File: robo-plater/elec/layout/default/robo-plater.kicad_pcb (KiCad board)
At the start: 2 copper layers, 80 parts, among them U1 ?, U10 ?, U11 ?, U12 ?, U13 ?, U14 ?, U15 ?, U16 ?, U17 ?, U18 ?, U19 ?, U2 ?, U3 ?, U4 ?, U5 ?, U6 ?, U7 ?, U8 ?, U9 ?

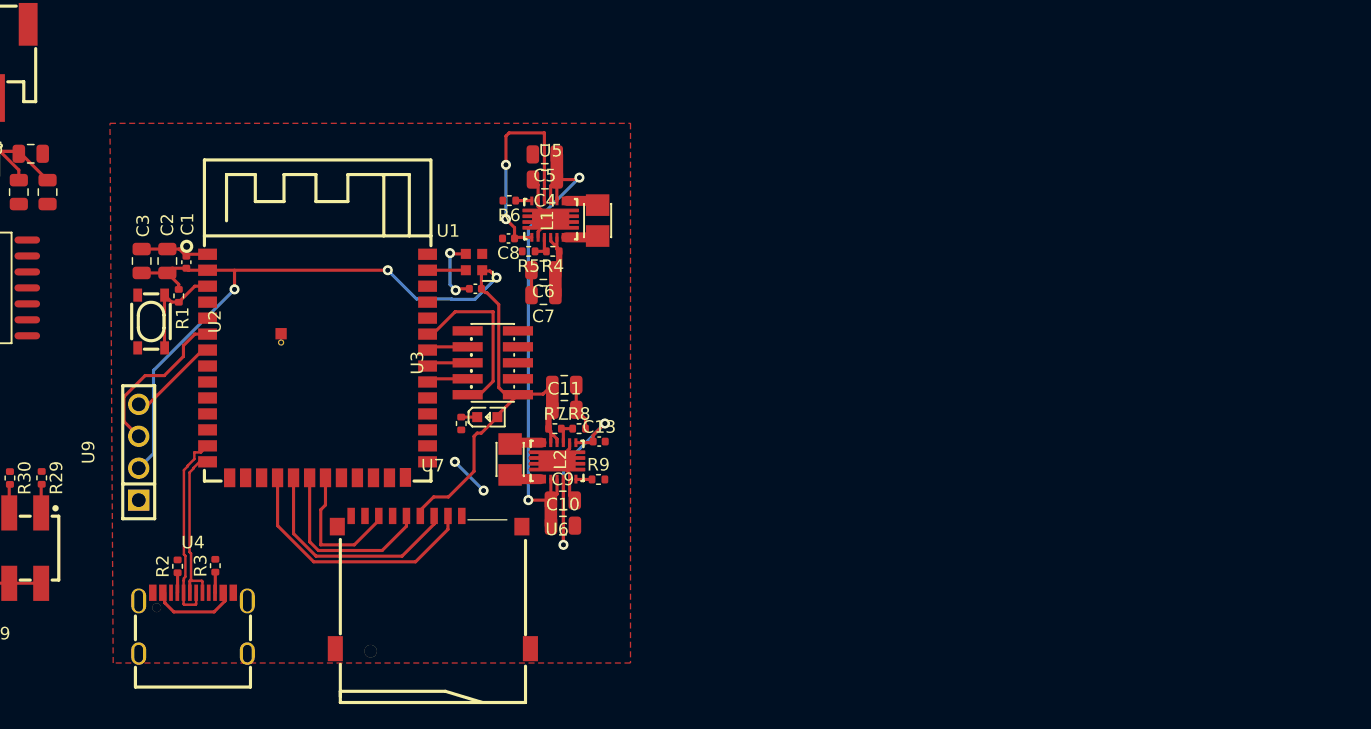
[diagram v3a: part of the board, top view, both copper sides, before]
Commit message: Add 12V input and power connector
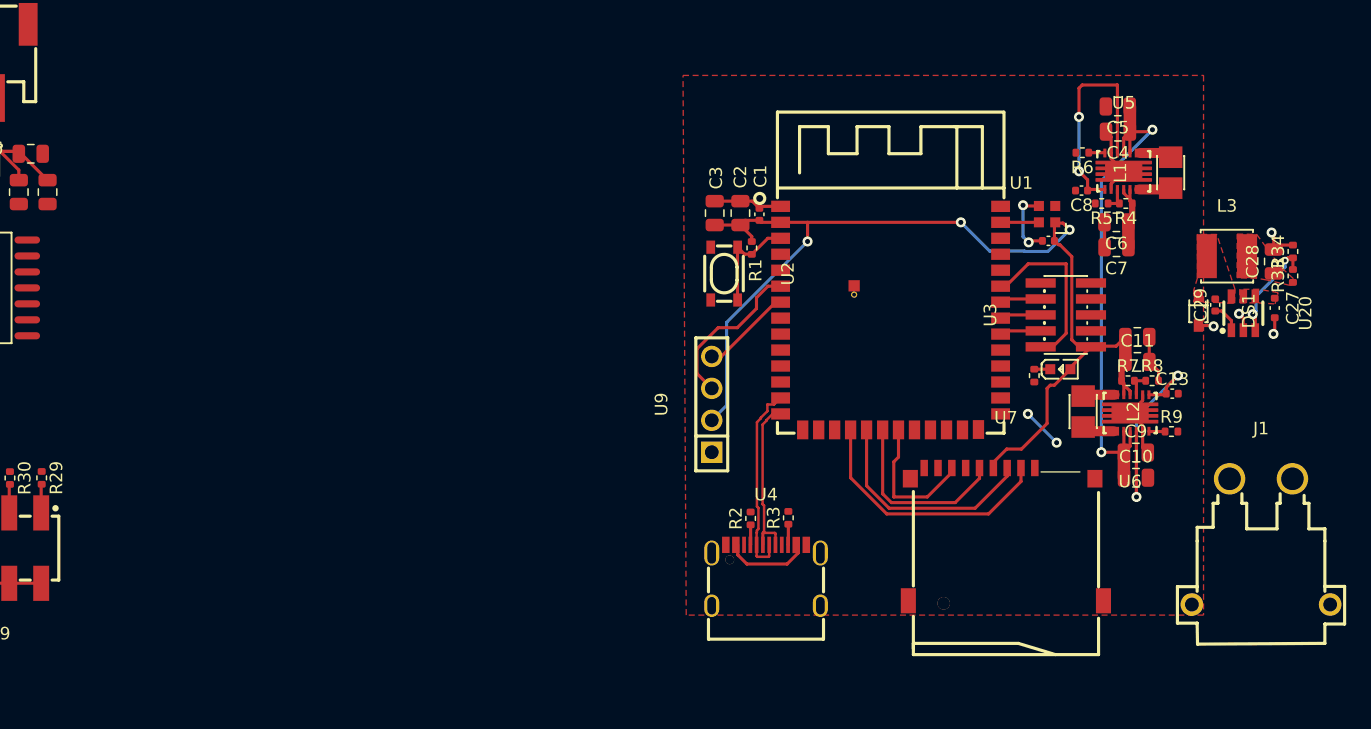
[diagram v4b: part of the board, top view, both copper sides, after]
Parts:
- added C27: 6.3V 10uF X5R ±20% 0402 Multilayer Ceramic Capacitors MLCC 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, lib:C0402, F.Cu at (196.4, 67.5)
- added C28: 25V 10uF X5R ±10% 0805 Multilayer Ceramic Capacitors MLCC -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, lib:C0805, F.Cu at (196.3, 63.8)
- added C29: 16V 100nF X7R ±10% 0402 Multilayer Ceramic Capacitors MLCC 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, lib:C0402, F.Cu at (191.7, 67.3)
- added DS1: ?, lib:SOD-323_L1.8-W1.3-LS2.5-RD, F.Cu at (190.3, 67.7)
- added J1: ?, lib:CONN-TH_XT30PW-M, F.Cu at (195.3, 86.1)
- added L3: ?, lib:IND-SMD_L4.0-W4.0, F.Cu at (192.6, 63.4)
- added R33: 62.5mW Thick Film Resistors 50V ±100ppm/℃ ±1% 23.7kΩ 0402 C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, lib:R0402, F.Cu at (197.9, 65.0)
- added R34: 62.5mW Thick Film Resistors 50V ±100ppm/℃ ±1% 4.3kΩ 0402 Ch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, lib:R0402, F.Cu at (197.9, 63.0)
- added U20: 0.6A, 42V, 1.1MHz Buck Regulator, lib:SOT-23-6_L2.9-W1.6-P0.95-LS2.8-BR, F.Cu at (193.9, 67.9)
- moved C12 45.7 mm to (185.5, 69.8)
- moved C13 45.7 mm to (188.3, 74.3)
- moved C2 45.7 mm to (153.9, 60.0)
- moved C6 45.7 mm to (183.8, 60.7)
- moved C9 45.7 mm to (185.4, 79.0)
- moved L1 45.7 mm to (188.1, 56.8)
- moved L2 45.7 mm to (181.2, 75.8)
- moved R1 45.7 mm to (154.8, 62.7)
- moved R10 45.7 mm to (177.3, 72.9)
- moved R4 45.7 mm to (184.6, 59.2)
- moved U3 45.7 mm to (179.8, 68.1)
- moved U6 45.7 mm to (184.9, 75.9)
- moved C1 45.7 mm to (155.4, 60.1)
- moved C3 45.7 mm to (151.9, 60.0)
- moved R2 45.7 mm to (154.7, 84.3)
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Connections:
- net uc.uc.ic-dm renamed ch2.pulses
- net uc.uc.ic-dm-1 renamed ch1.pulses
- net uc.uc.ic-dp renamed ch2.current
- net uc.uc.ic-dp-1 renamed ch1.current
- net uc.uc.ic-scl-2 renamed scl
- net uc.uc.ic-sda-2 renamed sda
- C1 pad 2: uc.uc.ic-gnd -> gnd
- C10 pad 2: uc.uc.ic-gnd -> gnd
- C11 pad 2: uc.uc.ic-gnd -> gnd
- C12 pad 2: uc.uc.ic-gnd -> gnd
- C13 pad 2: uc.uc.ic-gnd -> gnd
- C14 pad 2: uc.uc.ic-gnd -> gnd
- C2 pad 2: uc.uc.ic-gnd -> gnd
- C3 pad 2: uc.uc.ic-gnd -> gnd
- C4 pad 2: uc.uc.ic-gnd -> gnd
- C5 pad 2: uc.uc.ic-gnd -> gnd
- C6 pad 2: uc.uc.ic-gnd -> gnd
- C7 pad 2: uc.uc.ic-gnd -> gnd
- C8 pad 2: uc.uc.ic-gnd -> gnd
- C9 pad 2: uc.uc.ic-gnd -> gnd
- R10 pad 2: uc.uc.ic-gnd -> gnd
- R18 pad 1: uc.uc.ic-scl-1 -> ch1.dir
- R19 pad 1: uc.uc.ic-sda-1 -> ch1.pwm
- R2 pad 2: uc.uc.ic-gnd -> gnd
- R29 pad 1: uc.uc.ic-scl -> ch2.dir
- R3 pad 2: uc.uc.ic-gnd -> gnd
- R30 pad 1: uc.uc.ic-sda -> ch2.pwm
- R5 pad 2: uc.uc.ic-gnd -> gnd
- R6 pad 2: uc.uc.ic-gnd -> gnd
- R8 pad 2: uc.uc.ic-gnd -> gnd
- R9 pad 2: uc.uc.ic-gnd -> gnd
- U1 pad 1: uc.uc.ic-gnd -> gnd
- U1 pad 12: uc.uc.ic-sda -> ch2.dir
- U1 pad 15: uc.uc.ic-scl -> ch2.pwm
- U1 pad 40: uc.uc.ic-gnd -> gnd
- U1 pad 41: uc.uc.ic-gnd -> gnd
- U1 pad 8: uc.uc.ic-sda-1 -> ch1.dir
- U1 pad 9: uc.uc.ic-scl-1 -> ch1.pwm
- U10 pad 5: uc.uc.ic-scl-1 -> ch1.pwm
- U10 pad 6: uc.uc.ic-sda-1 -> ch1.dir
- U15 pad 5: uc.uc.ic-scl -> ch2.pwm
- U15 pad 6: uc.uc.ic-sda -> ch2.dir
- U2 pad 3: uc.uc.ic-gnd -> gnd
- U2 pad 4: uc.uc.ic-gnd -> gnd
- U3 pad 3: uc.uc.ic-gnd -> gnd
- U3 pad 5: uc.uc.ic-gnd -> gnd
- U3 pad 9: uc.uc.ic-gnd -> gnd
- U4 pad 1: uc.uc.ic-gnd -> gnd
- U4 pad 2: uc.uc.ic-gnd -> gnd
- U4 pad 3: uc.uc.ic-gnd -> gnd
- U4 pad 4: uc.uc.ic-gnd -> gnd
- U4 pad A1: uc.uc.ic-gnd -> gnd
- U4 pad A12: uc.uc.ic-gnd -> gnd
- U4 pad B1: uc.uc.ic-gnd -> gnd
- U4 pad B12: uc.uc.ic-gnd -> gnd
- U5 pad 13: uc.uc.ic-gnd -> gnd
- U5 pad 15: uc.uc.ic-gnd -> gnd
- U5 pad 2: uc.uc.ic-gnd -> gnd
- U6 pad 13: uc.uc.ic-gnd -> gnd
- U6 pad 15: uc.uc.ic-gnd -> gnd
- U6 pad 2: uc.uc.ic-gnd -> gnd
- U7 pad 10: uc.uc.ic-gnd -> gnd
- U7 pad 11: uc.uc.ic-gnd -> gnd
- U7 pad 12: uc.uc.ic-gnd -> gnd
- U7 pad 13: uc.uc.ic-gnd -> gnd
- U7 pad 6: uc.uc.ic-gnd -> gnd
- U8 pad 3: uc.uc.ic-gnd -> gnd
- U9 pad 1: uc.uc.ic-gnd -> gnd
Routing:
- net gnd: track 26.9 -> 62.0 mm, vias 0 -> 6
- net uc.uc.ic-gnd: track 28.1 -> 0.00 mm, vias 2 -> 0
- net uc.uc.ic-sda: track 14.2 -> 0.00 mm
- net ch2.dir: track 0.00 -> 14.2 mm
- net uc.uc.ic-sda-1: track 14.2 -> 0.00 mm
- net ch1.dir: track 0.00 -> 14.2 mm
- net uc.uc.ic-scl: track 14.2 -> 0.00 mm
- net ch2.pwm: track 0.00 -> 14.2 mm
- net uc.uc.ic-scl-1: track 14.2 -> 0.00 mm
- net ch1.pwm: track 0.00 -> 14.2 mm
- net supply_5v.feedback_div-out: track 0.00 -> 8.33 mm, vias 0 -> 2
- net cb: track 0.00 -> 2.36 mm
- added copper zone on F.Cu, net gnd
- added copper zone on F.Cu, net sw
- added copper zone on F.Cu, net uc-vcc
- added copper zone on F.Cu, net vcc
- removed copper zone on F.Cu, net uc.uc.ic-gnd

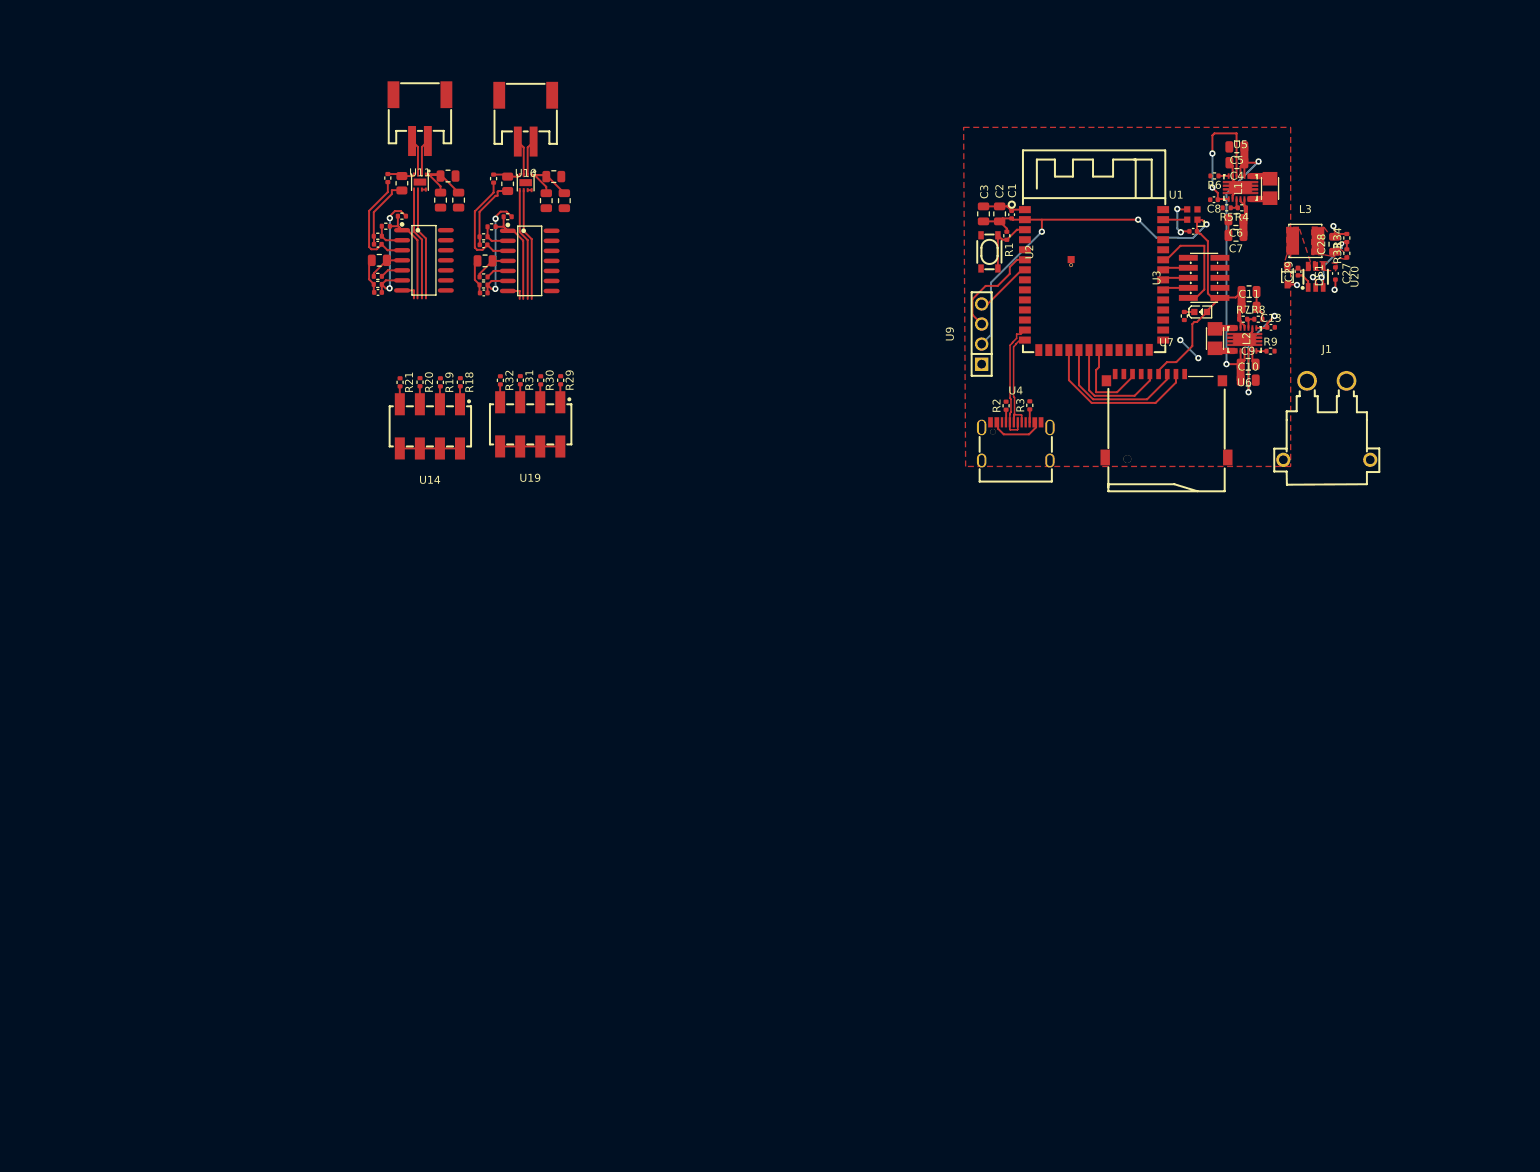
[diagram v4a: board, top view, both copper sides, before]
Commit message: Add io expander
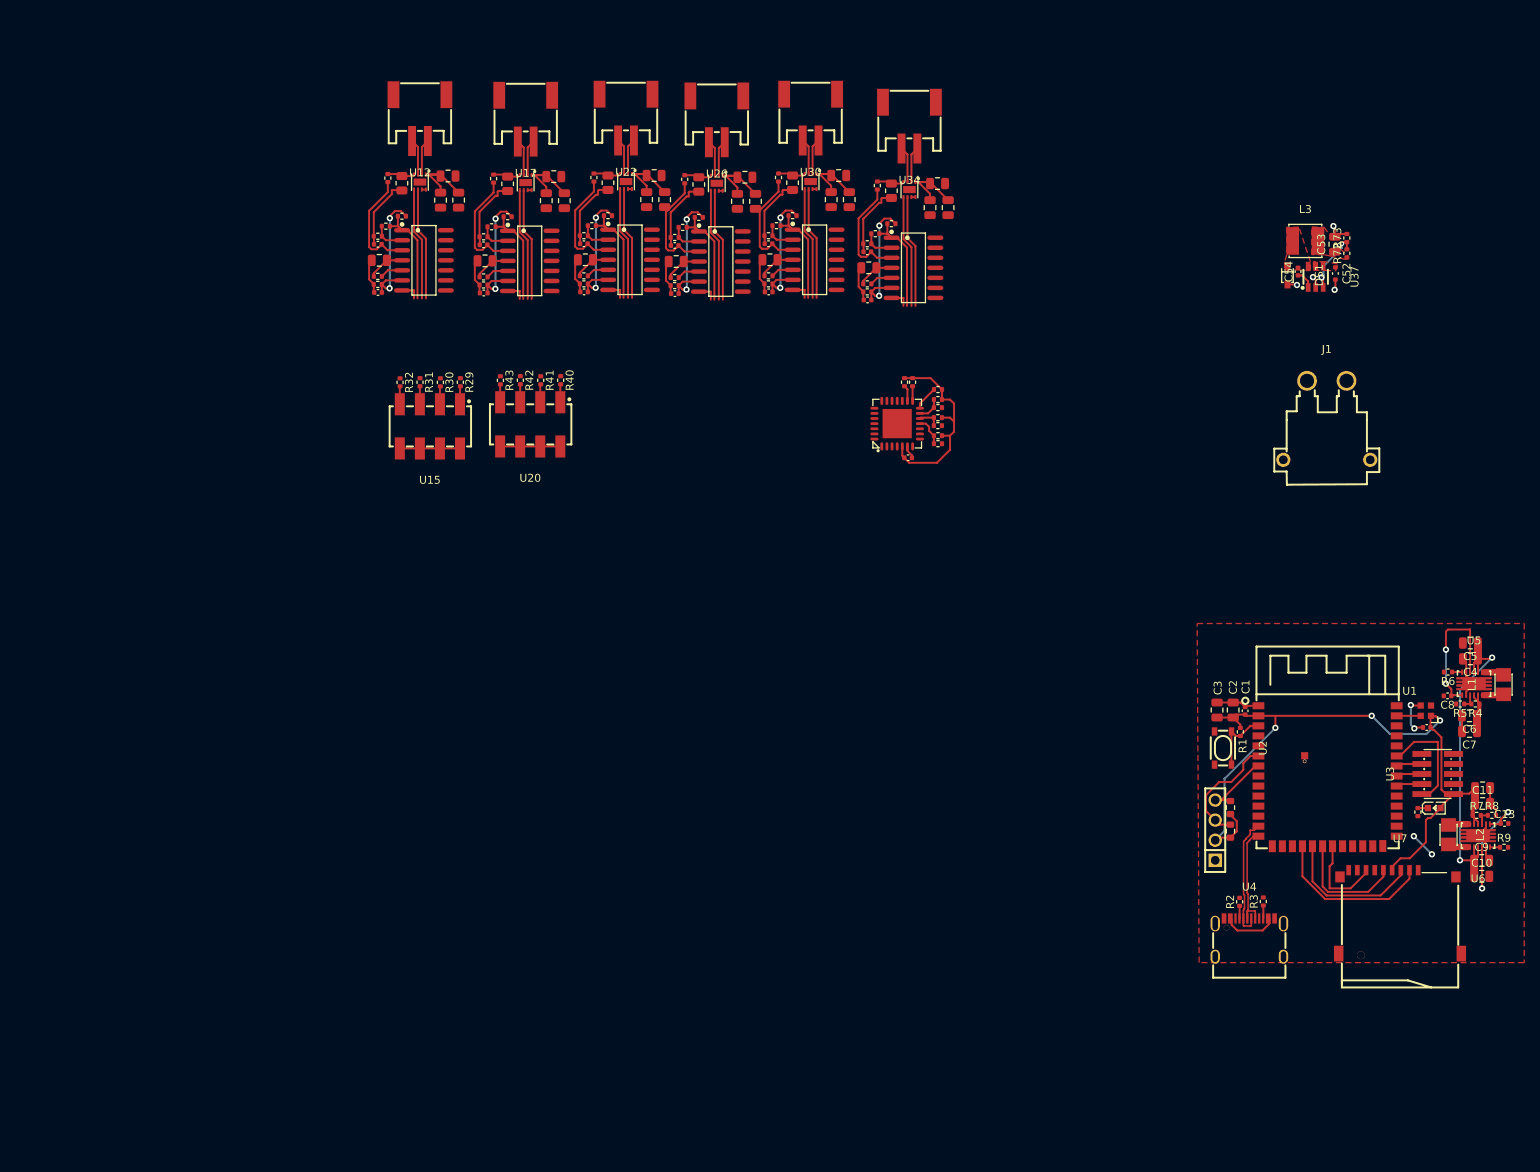
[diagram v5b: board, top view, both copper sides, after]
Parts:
- added C15: 16V 100nF X7R ±10% 0402 Multilayer Ceramic Capacitors MLCC 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, lib:C0402, F.Cu at (142.3, 90.8)
- added C28: 25V 10uF X5R ±10% 0805 Multilayer Ceramic Capacitors MLCC -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, lib:C0805, F.Cu at (111.5, 58.2)
- added C29: 25V 10uF X5R ±10% 0805 Multilayer Ceramic Capacitors MLCC -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, lib:C0805, F.Cu at (109.2, 58.2)
- added C30: 25V 10uF X5R ±10% 0805 Multilayer Ceramic Capacitors MLCC -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, lib:C0805, F.Cu at (110.2, 55.1)
- added C31: 25V 10uF X5R ±10% 0805 Multilayer Ceramic Capacitors MLCC -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, lib:C0805, F.Cu at (101.5, 65.8)
- added C32: 16V 100nF X7R ±10% 0402 Multilayer Ceramic Capacitors MLCC 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, lib:C0402, F.Cu at (101.3, 63.8)
- added C33: 25V 1uF X5R ±10% 0402 Multilayer Ceramic Capacitors MLCC - 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, lib:C0402, F.Cu at (101.3, 69.8)
- added C34: 25V 10uF X5R ±10% 0805 Multilayer Ceramic Capacitors MLCC -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, lib:C0805, F.Cu at (123.0, 58.4)
- added C35: 25V 10uF X5R ±10% 0805 Multilayer Ceramic Capacitors MLCC -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, lib:C0805, F.Cu at (120.7, 58.4)
- added C36: 25V 10uF X5R ±10% 0805 Multilayer Ceramic Capacitors MLCC -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, lib:C0805, F.Cu at (121.7, 55.3)
- added C37: 25V 10uF X5R ±10% 0805 Multilayer Ceramic Capacitors MLCC -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, lib:C0805, F.Cu at (113.0, 66.0)
- added C38: 16V 100nF X7R ±10% 0402 Multilayer Ceramic Capacitors MLCC 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, lib:C0402, F.Cu at (112.8, 64.0)
- added C39: 25V 1uF X5R ±10% 0402 Multilayer Ceramic Capacitors MLCC - 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, lib:C0402, F.Cu at (112.8, 70.1)
- added C40: 25V 10uF X5R ±10% 0805 Multilayer Ceramic Capacitors MLCC -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, lib:C0805, F.Cu at (134.9, 58.2)
- added C41: 25V 10uF X5R ±10% 0805 Multilayer Ceramic Capacitors MLCC -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, lib:C0805, F.Cu at (132.6, 58.2)
- added C42: 25V 10uF X5R ±10% 0805 Multilayer Ceramic Capacitors MLCC -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, lib:C0805, F.Cu at (133.5, 55.1)
- added C43: 25V 10uF X5R ±10% 0805 Multilayer Ceramic Capacitors MLCC -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, lib:C0805, F.Cu at (124.8, 65.8)
- added C44: 16V 100nF X7R ±10% 0402 Multilayer Ceramic Capacitors MLCC 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, lib:C0402, F.Cu at (124.6, 63.8)
- added C45: 25V 1uF X5R ±10% 0402 Multilayer Ceramic Capacitors MLCC - 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, lib:C0402, F.Cu at (124.7, 69.8)
- added C46: 25V 10uF X5R ±10% 0805 Multilayer Ceramic Capacitors MLCC -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, lib:C0805, F.Cu at (147.4, 59.2)
- added C47: 25V 10uF X5R ±10% 0805 Multilayer Ceramic Capacitors MLCC -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, lib:C0805, F.Cu at (145.1, 59.2)
- added C48: 25V 10uF X5R ±10% 0805 Multilayer Ceramic Capacitors MLCC -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, lib:C0805, F.Cu at (146.1, 56.1)
- added C49: 25V 10uF X5R ±10% 0805 Multilayer Ceramic Capacitors MLCC -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, lib:C0805, F.Cu at (137.3, 66.8)
- added C50: 16V 100nF X7R ±10% 0402 Multilayer Ceramic Capacitors MLCC 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, lib:C0402, F.Cu at (137.2, 64.8)
- added C51: 25V 1uF X5R ±10% 0402 Multilayer Ceramic Capacitors MLCC - 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, lib:C0402, F.Cu at (137.2, 70.9)
- added R11: 100mW Thick Film Resistors 75V ±100ppm/℃ ±1% 2.7kΩ 0603 Chi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, lib:R0603, F.Cu at (183.1, 135.1)
- added R12: 100mW Thick Film Resistors 75V ±100ppm/℃ ±1% 2.7kΩ 0603 Chi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, lib:R0603, F.Cu at (183.1, 138.1)
- added R13: 62.5mW Thick Film Resistors 50V ±100ppm/℃ ±1% 10kΩ 0402 Chi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, lib:R0402, F.Cu at (146.1, 88.1)
- added R14: 62.5mW Thick Film Resistors 50V ±100ppm/℃ ±1% 10kΩ 0402 Chi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, lib:R0402, F.Cu at (146.1, 89.1)
- added R15: 62.5mW Thick Film Resistors 50V ±100ppm/℃ ±1% 10kΩ 0402 Chi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, lib:R0402, F.Cu at (146.1, 85.8)
- added R16: 62.5mW Thick Film Resistors 50V ±100ppm/℃ ±1% 10kΩ 0402 Chi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, lib:R0402, F.Cu at (146.1, 86.8)
- added R17: 62.5mW Thick Film Resistors 50V ±100ppm/℃ ±1% 10kΩ 0402 Chi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, lib:R0402, F.Cu at (146.1, 83.5)
- added R18: 62.5mW Thick Film Resistors 50V ±100ppm/℃ ±1% 10kΩ 0402 Chi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, lib:R0402, F.Cu at (146.1, 84.5)
- added R19: 62.5mW Thick Film Resistors 50V ±100ppm/℃ ±1% 10kΩ 0402 Chi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, lib:R0402, F.Cu at (146.1, 82.2)
- added R20: 62.5mW Thick Film Resistors 50V ±100ppm/℃ ±1% 10kΩ 0402 Chi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, lib:R0402, F.Cu at (141.9, 81.3)
- added R21: 62.5mW Thick Film Resistors 50V ±100ppm/℃ ±1% 10kΩ 0402 Chi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, lib:R0402, F.Cu at (142.9, 81.3)
- added R44: 125mW Thick Film Resistors 150V ±1% ±400ppm/℃ 1Ω 0805 Chip 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, lib:R0805, F.Cu at (104.3, 56.0)
- added R45: 62.5mW Thick Film Resistors 50V ±100ppm/℃ ±1% 1.33kΩ 0402 C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, lib:R0402, F.Cu at (102.5, 55.4)
- added R46: 62.5mW Thick Film Resistors 50V ±100ppm/℃ ±1% 365Ω 0402 Chi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, lib:R0402, F.Cu at (102.3, 61.5)
- added R47: 62.5mW Thick Film Resistors 50V ±100ppm/℃ ±1% 36.5Ω 0402 Ch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, lib:R0402, F.Cu at (101.3, 62.7)
- added R48: 62.5mW Thick Film Resistors 50V ±100ppm/℃ ±1% 1.05kΩ 0402 C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, lib:R0402, F.Cu at (104.3, 60.2)
- added R49: 62.5mW Thick Film Resistors 50V ±100ppm/℃ ±1% 1MΩ 0402 Chip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, lib:R0402, F.Cu at (101.3, 67.8)
- added R50: 62.5mW Thick Film Resistors 50V ±100ppm/℃ ±1% 1MΩ 0402 Chip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, lib:R0402, F.Cu at (101.3, 68.8)
- added R51: 125mW Thick Film Resistors 150V ±1% ±400ppm/℃ 1Ω 0805 Chip 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, lib:R0805, F.Cu at (115.8, 56.2)
- added R52: 62.5mW Thick Film Resistors 50V ±100ppm/℃ ±1% 1.33kΩ 0402 C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, lib:R0402, F.Cu at (114.0, 55.6)
- added R53: 62.5mW Thick Film Resistors 50V ±100ppm/℃ ±1% 365Ω 0402 Chi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, lib:R0402, F.Cu at (113.8, 61.7)
- added R54: 62.5mW Thick Film Resistors 50V ±100ppm/℃ ±1% 36.5Ω 0402 Ch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, lib:R0402, F.Cu at (112.8, 63.0)
- added R55: 62.5mW Thick Film Resistors 50V ±100ppm/℃ ±1% 1.05kΩ 0402 C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, lib:R0402, F.Cu at (115.8, 60.4)
- added R56: 62.5mW Thick Film Resistors 50V ±100ppm/℃ ±1% 1MΩ 0402 Chip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, lib:R0402, F.Cu at (112.8, 68.0)
- added R57: 62.5mW Thick Film Resistors 50V ±100ppm/℃ ±1% 1MΩ 0402 Chip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, lib:R0402, F.Cu at (112.8, 69.1)
- added R58: 125mW Thick Film Resistors 150V ±1% ±400ppm/℃ 1Ω 0805 Chip 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, lib:R0805, F.Cu at (127.7, 56.0)
- added R59: 62.5mW Thick Film Resistors 50V ±100ppm/℃ ±1% 1.33kΩ 0402 C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, lib:R0402, F.Cu at (125.9, 55.4)
- added R60: 62.5mW Thick Film Resistors 50V ±100ppm/℃ ±1% 365Ω 0402 Chi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, lib:R0402, F.Cu at (125.7, 61.5)
- added R61: 62.5mW Thick Film Resistors 50V ±100ppm/℃ ±1% 36.5Ω 0402 Ch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, lib:R0402, F.Cu at (124.6, 62.7)
- added R62: 62.5mW Thick Film Resistors 50V ±100ppm/℃ ±1% 1.05kΩ 0402 C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, lib:R0402, F.Cu at (127.7, 60.2)
- added R63: 62.5mW Thick Film Resistors 50V ±100ppm/℃ ±1% 1MΩ 0402 Chip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, lib:R0402, F.Cu at (124.7, 67.8)
- added R64: 62.5mW Thick Film Resistors 50V ±100ppm/℃ ±1% 1MΩ 0402 Chip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, lib:R0402, F.Cu at (124.6, 68.8)
- added R65: 125mW Thick Film Resistors 150V ±1% ±400ppm/℃ 1Ω 0805 Chip 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, lib:R0805, F.Cu at (140.2, 57.0)
- added R66: 62.5mW Thick Film Resistors 50V ±100ppm/℃ ±1% 1.33kΩ 0402 C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, lib:R0402, F.Cu at (138.4, 56.4)
- added R67: 62.5mW Thick Film Resistors 50V ±100ppm/℃ ±1% 365Ω 0402 Chi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, lib:R0402, F.Cu at (138.2, 62.5)
- added R68: 62.5mW Thick Film Resistors 50V ±100ppm/℃ ±1% 36.5Ω 0402 Ch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, lib:R0402, F.Cu at (137.2, 63.8)
- added R69: 62.5mW Thick Film Resistors 50V ±100ppm/℃ ±1% 1.05kΩ 0402 C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, lib:R0402, F.Cu at (140.2, 61.2)
- added R70: 62.5mW Thick Film Resistors 50V ±100ppm/℃ ±1% 1MΩ 0402 Chip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, lib:R0402, F.Cu at (137.2, 68.8)
- added R71: 62.5mW Thick Film Resistors 50V ±100ppm/℃ ±1% 1MΩ 0402 Chip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, lib:R0402, F.Cu at (137.2, 69.8)
- added U10: ?, lib:QFN-28_L6.0-W6.0-P0.65-BL-EP3.7, F.Cu at (140.9, 86.5)
- added U21: ?, lib:WSON-8_L2.0-W2.0-P0.50-TL-EP, F.Cu at (106.6, 55.9)
- added U22: ?, lib:CONN-SMD_P2.00_S2B-PH-SM4-TB-LF-SN, F.Cu at (106.6, 47.8)
- added U23: ?, lib:NetTie-2_SMD_Pad0.25mm, F.Cu at (103.1, 57.5)
- added U24: ?, lib:SOIC-14_L8.7-W3.9-P1.27-LS6.0-BL, F.Cu at (107.1, 65.8)
- added U25: ?, lib:WSON-8_L2.0-W2.0-P0.50-TL-EP, F.Cu at (118.1, 56.1)
- added U26: ?, lib:CONN-SMD_P2.00_S2B-PH-SM4-TB-LF-SN, F.Cu at (118.1, 48.0)
- added U27: ?, lib:NetTie-2_SMD_Pad0.25mm, F.Cu at (114.6, 57.8)
- added U28: ?, lib:SOIC-14_L8.7-W3.9-P1.27-LS6.0-BL, F.Cu at (118.6, 66.0)
- added U29: ?, lib:WSON-8_L2.0-W2.0-P0.50-TL-EP, F.Cu at (130.0, 55.9)
- added U30: ?, lib:CONN-SMD_P2.00_S2B-PH-SM4-TB-LF-SN, F.Cu at (130.0, 47.8)
- added U31: ?, lib:NetTie-2_SMD_Pad0.25mm, F.Cu at (126.4, 57.5)
- added U32: ?, lib:SOIC-14_L8.7-W3.9-P1.27-LS6.0-BL, F.Cu at (130.5, 65.8)
- added U33: ?, lib:WSON-8_L2.0-W2.0-P0.50-TL-EP, F.Cu at (142.5, 56.9)
- added U34: ?, lib:CONN-SMD_P2.00_S2B-PH-SM4-TB-LF-SN, F.Cu at (142.5, 48.8)
- added U35: ?, lib:NetTie-2_SMD_Pad0.25mm, F.Cu at (138.9, 58.6)
- added U36: ?, lib:SOIC-14_L8.7-W3.9-P1.27-LS6.0-BL, F.Cu at (143.0, 66.8)
- moved R10 69.4 mm to (206.9, 135.7)
- moved U1 69.4 mm to (195.4, 131.1)
- moved C1 69.4 mm to (185.0, 122.9)
- moved C10 69.4 mm to (214.9, 143.8)
- moved C11 69.4 mm to (215.1, 134.6)
- moved C12 69.4 mm to (215.0, 132.6)
- moved C13 69.4 mm to (217.8, 137.1)
- moved C14 69.4 mm to (208.0, 125.0)
- moved C2 69.4 mm to (183.5, 122.8)
- moved C3 69.4 mm to (181.4, 122.8)
- moved C4 69.4 mm to (213.5, 116.3)
- moved C5 69.4 mm to (213.5, 114.3)
- moved C6 69.4 mm to (213.4, 123.5)
- moved C7 69.4 mm to (213.4, 125.5)
- moved C8 69.4 mm to (210.6, 121.0)
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- renumbered C15 to C16, C16 to C17, C17 to C18, C18 to C19, C19 to C20, C20 to C21, C21 to C22, C22 to C23, C23 to C24, C24 to C25, C25 to C26, C26 to C27, C27 to C52, C28 to C53, C29 to C54, R11 to R22, R12 to R23, R13 to R24, R14 to R25, R15 to R26, R16 to R27, R17 to R28, R18 to R29, R19 to R30, R20 to R31, R21 to R32, R22 to R33, R23 to R34, R24 to R35, R25 to R36, R26 to R37, R27 to R38, R28 to R39, R29 to R40, R30 to R41, R31 to R42, R32 to R43, R33 to R72, R34 to R73, U10 to U11, U11 to U12, U12 to U13, U13 to U14, U14 to U15, U15 to U16, U16 to U17, U17 to U18, U18 to U19, U19 to U20, U20 to U37
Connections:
- net reset renamed uc.uc-reset
- C1 pad 1: uc.uc.ic-vcc -> vcc-1
- C11 pad 1: uc.uc.ic-vcc -> vcc-1
- C12 pad 1: uc.uc.ic-vcc -> vcc-1
- C14 pad 1: uc.uc.ic-vcc -> vcc-1
- C2 pad 1: uc.uc.ic-vcc -> vcc-1
- C3 pad 1: uc.uc.ic-vcc -> vcc-1
- LED1 pad 2: uc.uc.ic-vcc -> vcc-1
- R1 pad 1: uc.uc.ic-vcc -> vcc-1
- R7 pad 1: uc.uc.ic-vcc -> vcc-1
- U1 pad 16: io46 -> ch3.pulses
- U1 pad 2: uc.uc.ic-vcc -> vcc-1
- U1 pad 22: io14 -> ch3.pwm
- U1 pad 23: io21 -> ch4.pulses
- U1 pad 25: io48 -> ch4.pwm
- U1 pad 26: io45 -> ch5.pulses
- U1 pad 28: io35 -> ch5.pwm
- U1 pad 29: io36 -> ch6.pulses
- U1 pad 31: io38 -> ch6.pwm
- U3 pad 1: uc.uc.ic-vcc -> vcc-1
- U6 pad 4: uc.uc.ic-vcc -> vcc-1
- U6 pad 5: uc.uc.ic-vcc -> vcc-1
- U7 pad 4: uc.uc.ic-vcc -> vcc-1
- U8 pad 1: uc.uc.ic-vcc -> vcc-1
- U9 pad 2: uc.uc.ic-vcc -> vcc-1
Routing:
- net vcc-1: track 10.3 -> 149.1 mm, vias 0 -> 3
- net uc.uc.ic-vcc: track 86.9 -> 0.00 mm, vias 3 -> 0
- net vcc: track 20.1 -> 60.2 mm
- net gnd: track 62.0 -> 87.1 mm
- net ch3.op_amp-in2_minus: track 0.00 -> 16.7 mm, vias 0 -> 2
- net ch5.op_amp-in2_minus: track 0.00 -> 16.7 mm, vias 0 -> 2
- net ch4.op_amp-in2_minus: track 0.00 -> 16.7 mm, vias 0 -> 2
- net ch6.op_amp-in2_minus: track 0.00 -> 16.7 mm, vias 0 -> 2
- net ch4.dir: track 0.00 -> 14.2 mm
- net ch6.dir: track 0.00 -> 14.2 mm
- net ch3.dir: track 0.00 -> 14.2 mm
- net ch5.dir: track 0.00 -> 14.2 mm
- net ch4.pwm: track 0.00 -> 14.2 mm
- net ch6.pwm: track 0.00 -> 14.2 mm
- net ch5.pwm: track 0.00 -> 14.2 mm
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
